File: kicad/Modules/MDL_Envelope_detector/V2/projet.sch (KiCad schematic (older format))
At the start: 10 parts, among them T1 2N2222, T2 2N2907A, T3 2N2907A

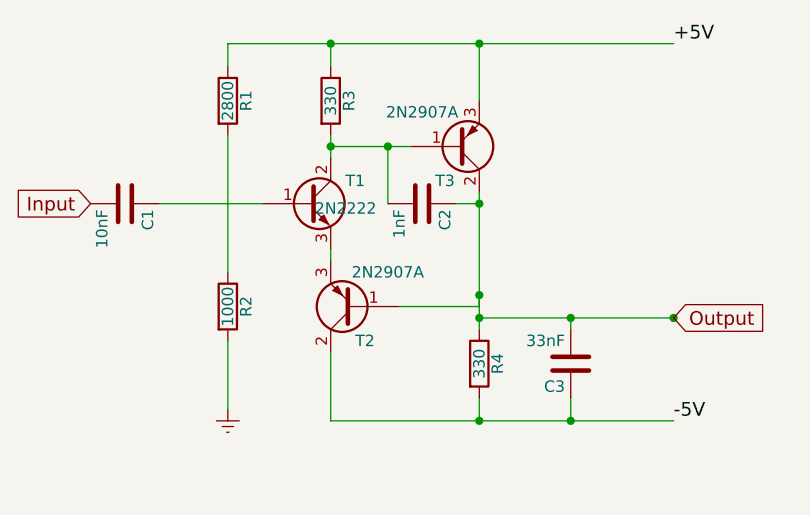
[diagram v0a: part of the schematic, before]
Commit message: update DB_HV, update librairy and librairy path for MDL
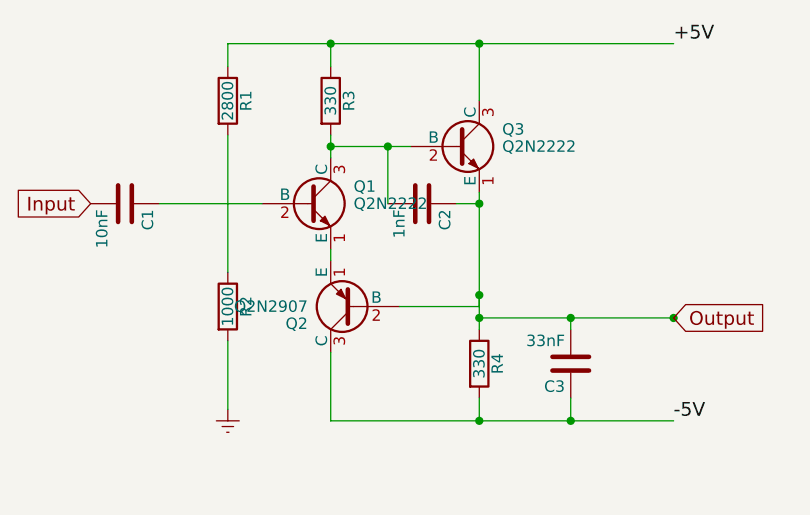
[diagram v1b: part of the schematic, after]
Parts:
- removed T1: 2N2222, symbol Q_NPN_BCE
- removed T2, T3: 2N2907A, symbol Q_PNP_BCE
- added Q1, Q3: Q2N2222, symbol Q2N2222
- added Q2: Q2N2907, symbol Q2N2907
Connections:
- net +5V: now also Q3.3 (C)
- net -5V: now also Q2.3 (C)
- net Output: now also Q2.2 (B), Q3.1 (E)
- net at C1.1: now also Q1.2 (B)
- net at C2.2, R3.2: now also Q1.3 (C), Q3.2 (B)
- new net: Q1.1 (E), Q2.1 (E)
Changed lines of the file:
@@
 LIBS:contrib
 LIBS:valves
+LIBS:echopen
 LIBS:projet-cache
 EELAYER 25 0
@@
 	1    0    0    -1
 $EndComp
-$Comp
-L Q_NPN_BCE T1
-U 1 1 576BE9ED
-P 5600 3850
-F 0 "T1" H 5850 3950 50  0000 R CNN
-F 1 "2N2222" H 5900 3800 50  0000 R BNN
-F 2 "" H 5800 3950 50  0000 C CNN
-F 3 "" H 5600 3850 50  0000 C CNN
-	1    5600 3850
-	1    0    0    -1
-$EndComp
 Wire Wire Line
 	5250 3550 5250 4150
 Wire Wire Line
 	5400 3850 4950 3850
-$Comp
-L Q_PNP_BCE T2
-U 1 1 576BEED3
-P 5800 4300
-F 0 "T2" H 5750 4450 50  0000 C CNN
-F 1 "2N2907A" H 5650 4150 50  0000 C CNN
-F 2 "" H 6000 4400 50  0000 C CNN
-F 3 "" H 5800 4300 50  0000 C CNN
-	1    5800 4300
-	-1   0    0    1
-$EndComp
 $Comp
 L R R4
@@
 	1    6350 4550
 	1    0    0    -1
-$EndComp
-$Comp
-L Q_PNP_BCE T3
-U 1 1 576C07B0
-P 6250 3600
-F 0 "T3" H 6200 3750 50  0000 C CNN
-F 1 "2N2907A" H 6100 3450 50  0000 C CNN
-F 2 "" H 6450 3700 50  0000 C CNN
-F 3 "" H 6250 3600 50  0000 C CNN
-	1    6250 3600
-	1    0    0    1
 $EndComp
 Wire Wire Line
@@
 Text GLabel 7200 4350 2    60   Input ~ 0
 Output
+$Comp
+L Q2N2222 Q1
+U 1 1 57B43494
+P 5600 3850
+F 0 "Q1" H 5800 3925 50  0000 L CNN
+F 1 "Q2N2222" H 5800 3850 50  0000 L CNN
+F 2 "" H 5800 3775 50  0000 L CIN
+F 3 "" H 5600 3850 50  0000 L CNN
+	1    5600 3850
+	1    0    0    -1
+$EndComp
+$Comp
+L Q2N2907 Q2
+U 1 1 57B43524
+P 5800 4300
+F 0 "Q2" H 6000 4375 50  0000 L CNN
+F 1 "Q2N2907" H 6000 4300 50  0000 L CNN
+F 2 "" H 6100 4150 50  0000 L CIN
+F 3 "" H 5800 4300 50  0000 L CNN
+	1    5800 4300
+	-1   0    0    1
+$EndComp
+$Comp
+L Q2N2222 Q3
+U 1 1 57B435C4
+P 6250 3600
+F 0 "Q3" H 6450 3675 50  0000 L CNN
+F 1 "Q2N2222" H 6450 3600 50  0000 L CNN
+F 2 "" H 6450 3525 50  0000 L CIN
+F 3 "" H 6250 3600 50  0000 L CNN
+	1    6250 3600
+	1    0    0    -1
+$EndComp
 $EndSCHEMATC

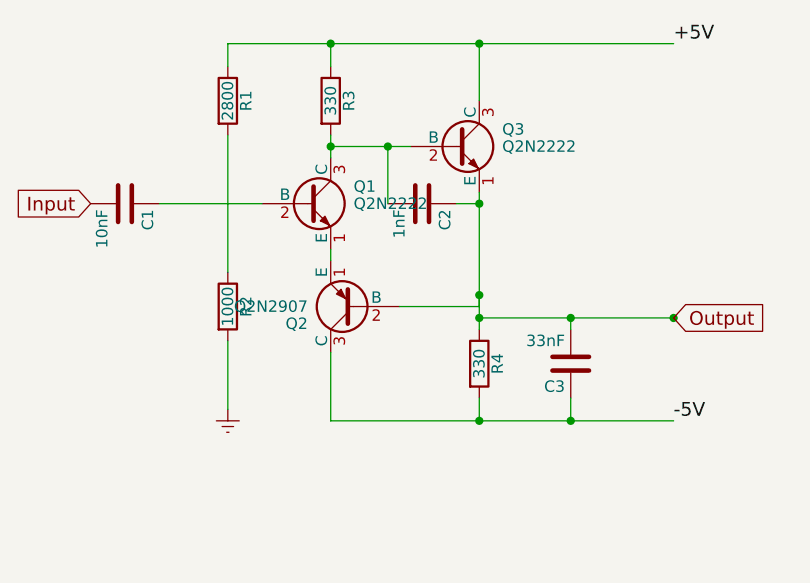
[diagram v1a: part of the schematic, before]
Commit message: update MDLs with new librairy
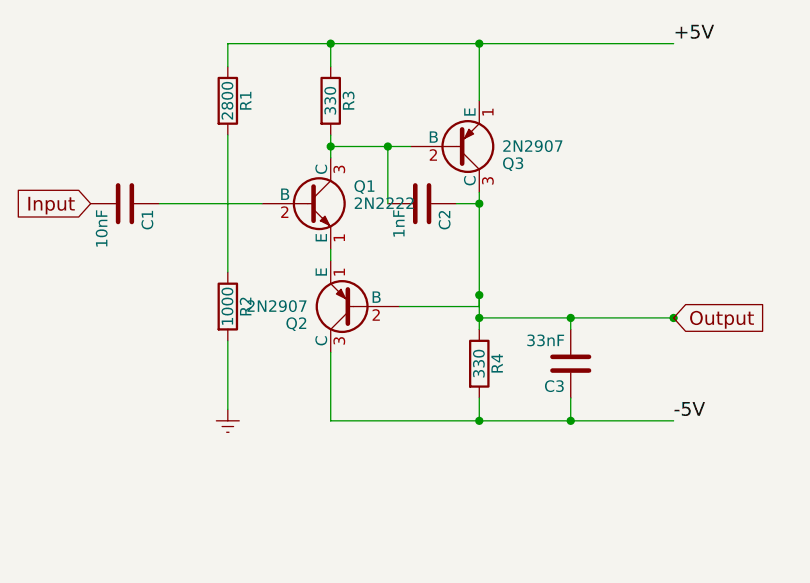
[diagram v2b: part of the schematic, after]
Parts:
- removed Q1, Q3: Q2N2222, symbol Q2N2222
- removed Q2: Q2N2907, symbol Q2N2907
- added Q1: 2N2222, symbol 2N2222
- added Q2, Q3: 2N2907, symbol 2N2907
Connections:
- net +5V: now also Q3.1 (E)
- net -5V: now also Q2.3 (C)
- net Output: now also Q2.2 (B), Q3.3 (C)
- net at C1.1: now also Q1.2 (B)
- net at C2.2, R3.2: now also Q1.3 (C), Q3.2 (B)
- new net: Q1.1 (E), Q2.1 (E)
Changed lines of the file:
@@
 Connection ~ 5700 3150
 Wire Wire Line
-	5700 3650 5700 3550
+	5700 3550 5700 3650
 Wire Wire Line
-	6050 3600 5700 3600
+	5700 3600 6050 3600
 Connection ~ 5700 3600
 Wire Wire Line
@@
 Connection ~ 6350 3850
 Wire Wire Line
-	6350 3400 6350 3150
+	6350 3150 6350 3400
 Connection ~ 6350 3150
 Wire Wire Line
@@
 $EndComp
 Wire Wire Line
-	6750 4700 6750 4800
+	6750 4800 6750 4700
 Connection ~ 6750 4800
 Wire Wire Line
@@
 Output
 $Comp
-L Q2N2222 Q1
-U 1 1 57B43494
+L 2N2222 Q1
+U 1 1 57B46EA7
 P 5600 3850
 F 0 "Q1" H 5800 3925 50  0000 L CNN
-F 1 "Q2N2222" H 5800 3850 50  0000 L CNN
+F 1 "2N2222" H 5800 3850 50  0000 L CNN
 F 2 "" H 5800 3775 50  0000 L CIN
 F 3 "" H 5600 3850 50  0000 L CNN
@@
 $EndComp
 $Comp
-L Q2N2907 Q2
-U 1 1 57B43524
+L 2N2907 Q3
+U 1 1 57B46EEB
+P 6250 3600
+F 0 "Q3" H 6450 3675 50  0000 L CNN
+F 1 "2N2907" H 6450 3600 50  0000 L CNN
+F 2 "" H 6550 3450 50  0000 L CIN
+F 3 "" H 6250 3600 50  0000 L CNN
+	1    6250 3600
+	1    0    0    1
+$EndComp
+$Comp
+L 2N2907 Q2
+U 1 1 57B46F66
 P 5800 4300
 F 0 "Q2" H 6000 4375 50  0000 L CNN
-F 1 "Q2N2907" H 6000 4300 50  0000 L CNN
+F 1 "2N2907" H 6000 4300 50  0000 L CNN
 F 2 "" H 6100 4150 50  0000 L CIN
 F 3 "" H 5800 4300 50  0000 L CNN
@@
 	-1   0    0    1
 $EndComp
-$Comp
-L Q2N2222 Q3
-U 1 1 57B435C4
-P 6250 3600
-F 0 "Q3" H 6450 3675 50  0000 L CNN
-F 1 "Q2N2222" H 6450 3600 50  0000 L CNN
-F 2 "" H 6450 3525 50  0000 L CIN
-F 3 "" H 6250 3600 50  0000 L CNN
-	1    6250 3600
-	1    0    0    -1
-$EndComp
 $EndSCHEMATC
